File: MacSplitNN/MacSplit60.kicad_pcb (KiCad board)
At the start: 2 copper layers, 166.1 x 112 mm, 75 parts, among them J1 AudioJack4, SW1 SW_Push, SW10 SW_Push, SW100 Toggle Mac/Win, SW11 SW_Push, SW12 SW_Push, SW13 SW_Push, SW14 SW_Push, SW15 SW_Push, SW16 SW_Push, SW17 SW_Push, SW18 SW_Push, SW19 SW_Push, SW2 SW_Push, SW20 SW_Push, SW21 SW_Push, SW22 SW_Push, SW23 SW_Push, SW24 SW_Push, SW25 SW_Push, SW26 SW_Push, SW27 SW_Push, SW28 SW_Push, SW29 SW_Push, SW3 SW_Push, SW30 SW_Push, SW4 SW_Push, SW5 SW_Push, SW6 SW_Push, SW7 SW_Push, SW8 SW_Push, SW9 SW_Push, U2 KB2040

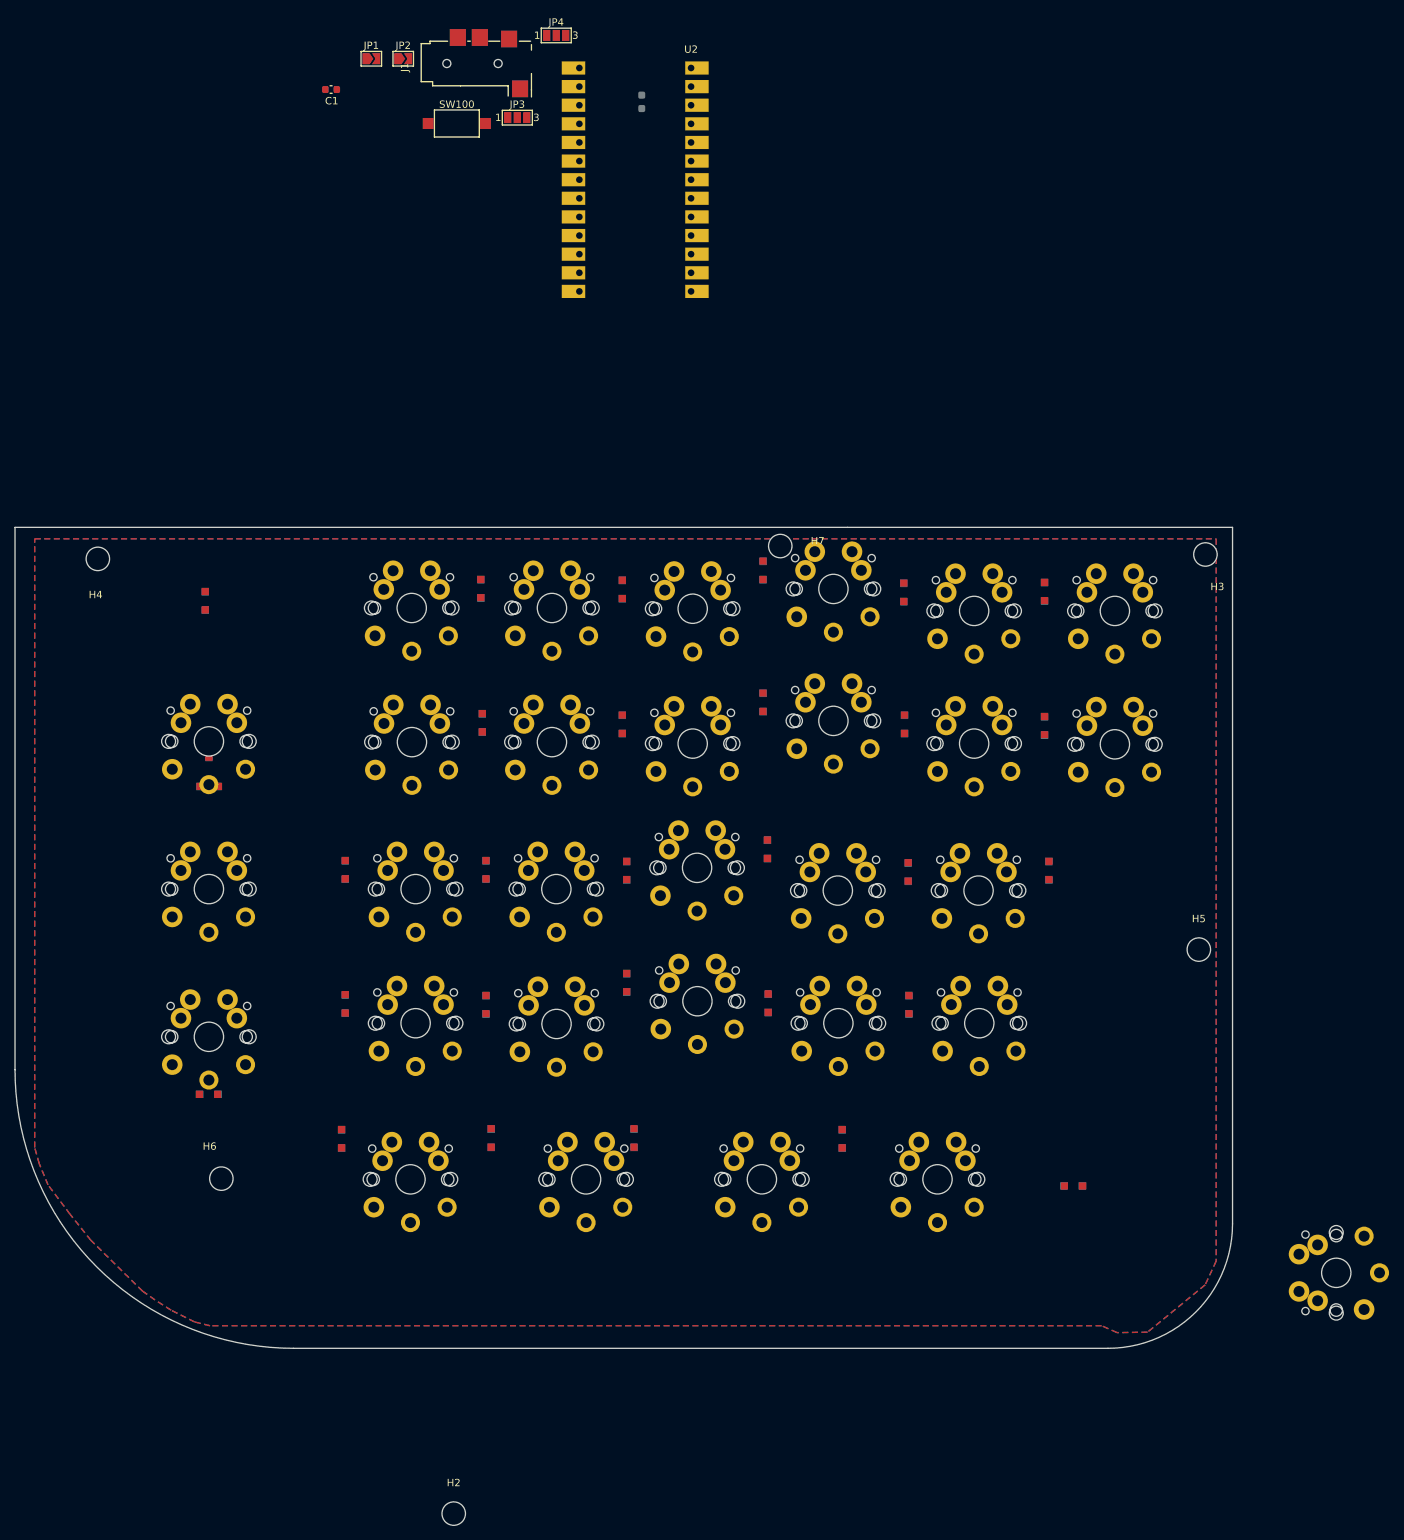
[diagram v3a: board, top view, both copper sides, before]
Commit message: Aligns rows and columns of switches
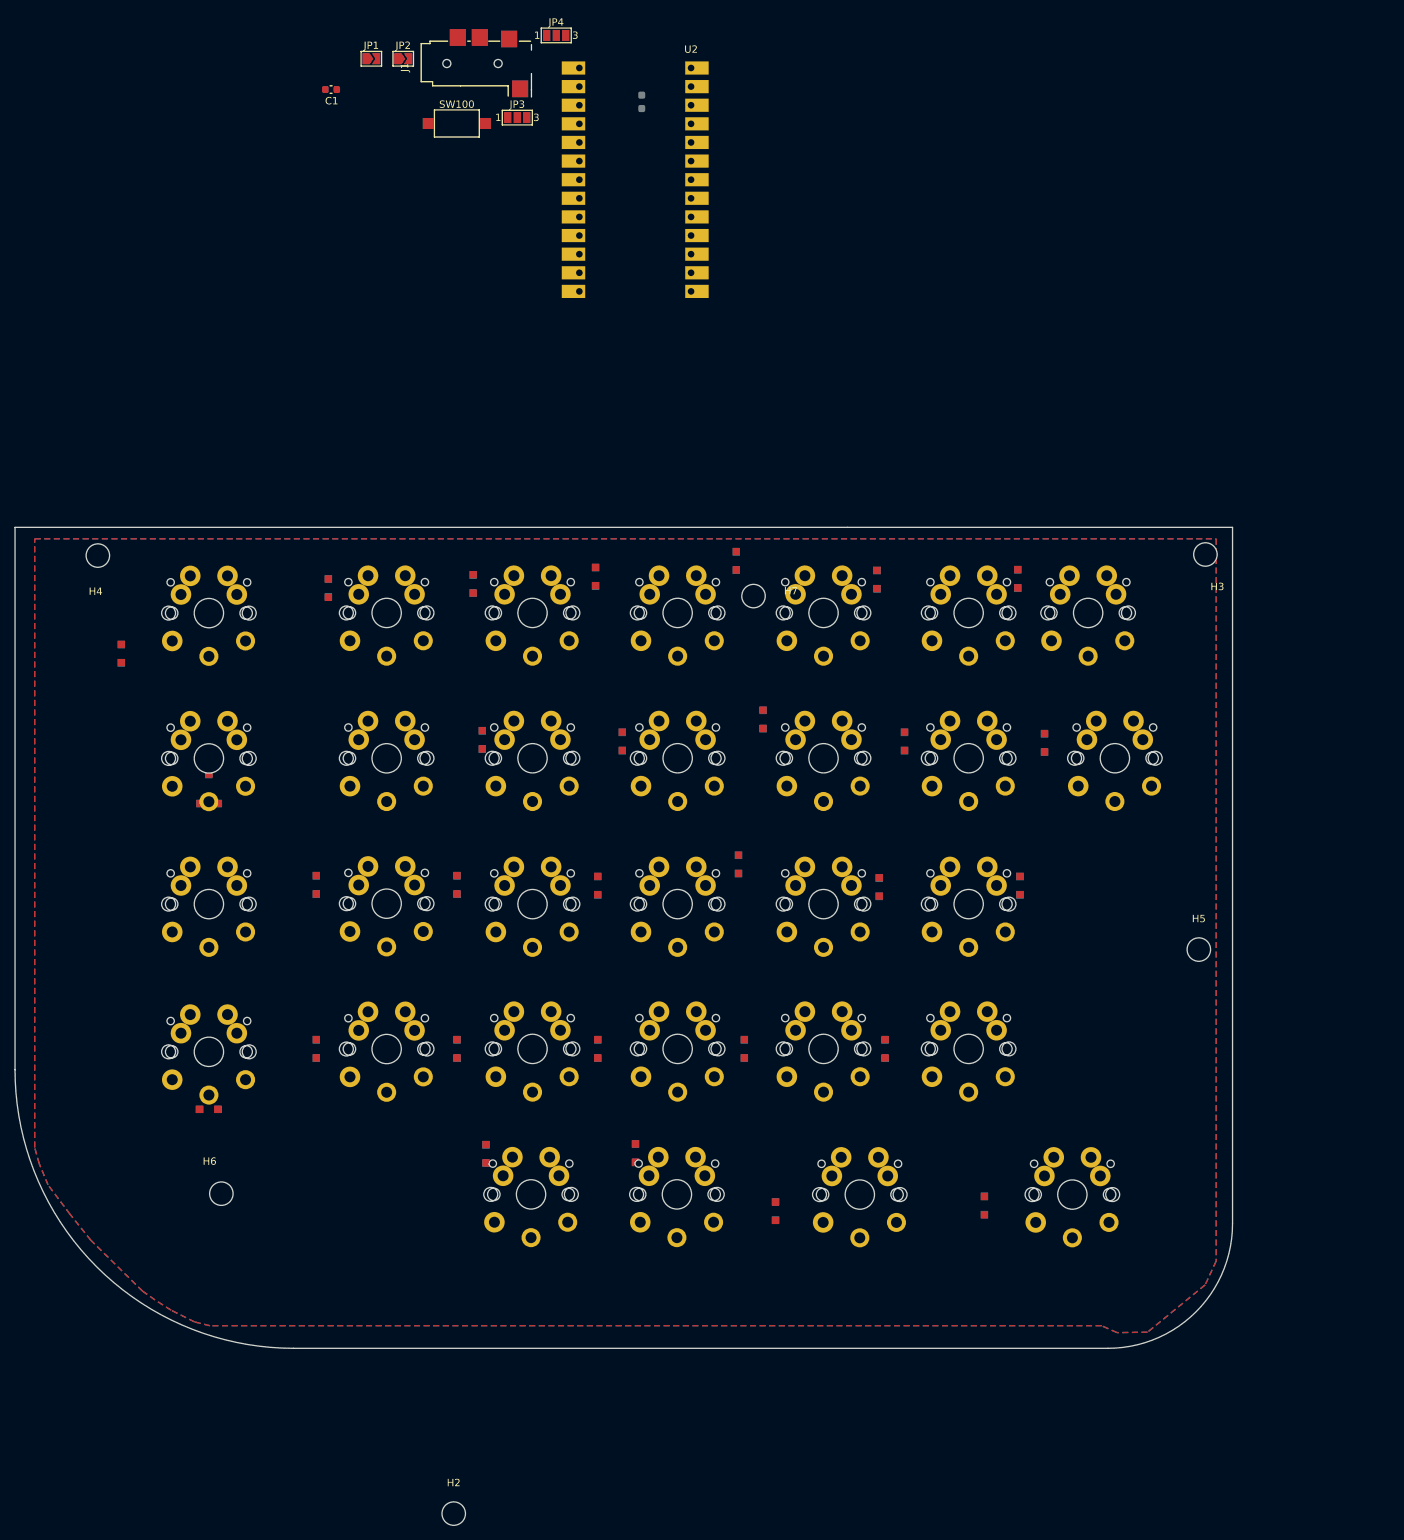
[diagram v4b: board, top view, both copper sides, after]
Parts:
- moved SW29 178.2 mm to (113.0, 46.7), turned to 0 degrees
- moved D32 148.8 mm to (101.0, 52.2), turned to 90 degrees
- moved D30 21.7 mm to (190.2, 128.2), turned to -90 degrees
- moved D31 21.4 mm to (218.8, 127.5), turned to -90 degrees
- moved D29 19.8 mm to (171.2, 120.4)
- moved D28 19.8 mm to (150.8, 120.5)
- moved SW28 18.5 mm to (230.8, 126.0)
- moved D1 16.9 mm to (129.2, 43.2), turned to -90 degrees
- moved SW25 16.6 mm to (156.9, 126.0)
- moved SW27 13.5 mm to (201.8, 126.0)
- moved SW26 12.6 mm to (176.8, 126.0)
- moved D25 9.85 mm to (166.0, 106.2)
- moved H7 7.74 mm to (187.2, 44.4)
- moved D23 7.29 mm to (127.6, 106.2)
- moved D24 7.20 mm to (146.8, 106.2)
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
